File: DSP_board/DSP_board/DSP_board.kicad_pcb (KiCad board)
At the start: 2 copper layers, 67 parts, among them IC1 74LCX125MTCX, IC2 74LCX125MTCX, IC3 74LCX125MTCX, IC4 74LCX125MTCX, U1 AM264LAUNCH

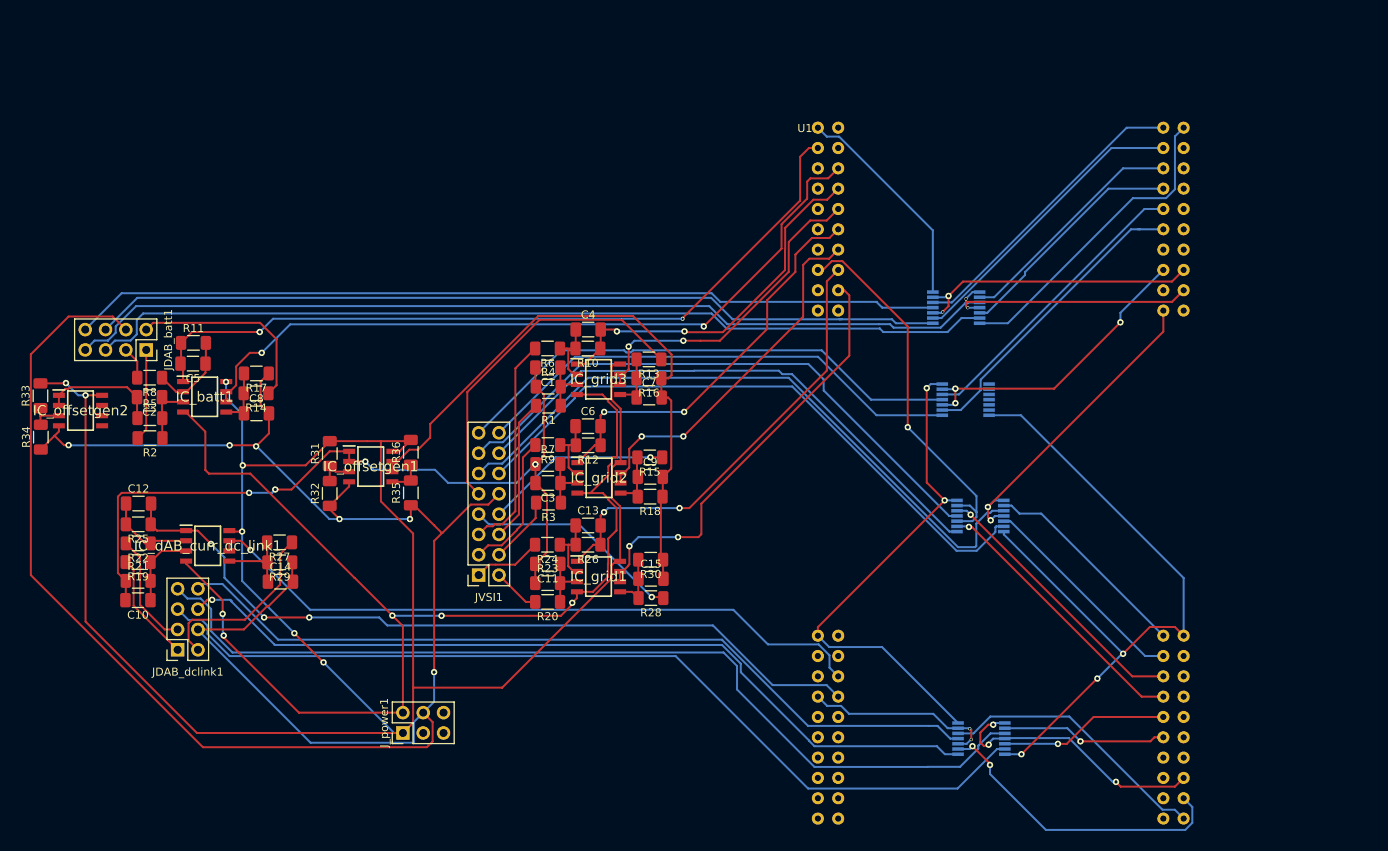
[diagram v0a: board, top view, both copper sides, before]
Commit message: including FPGA
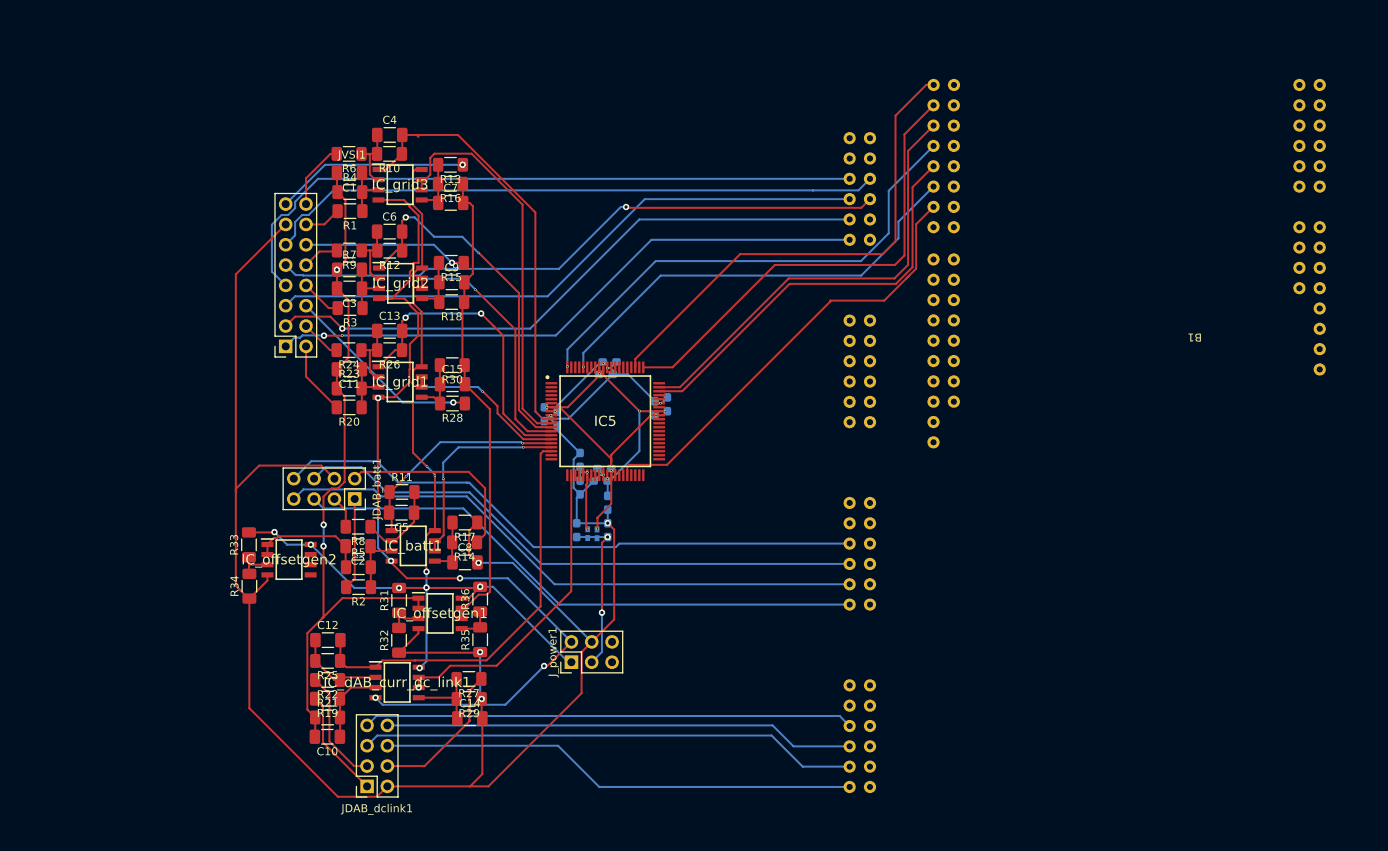
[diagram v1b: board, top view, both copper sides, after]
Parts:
- removed IC1, IC2, IC3, IC4: 74LCX125MTCX, 74125:SOP65P640X120-14N
- removed U1: AM264LAUNCH, am263x_devboard:AM2634_LAUNCH
- added B1: Arty-S7, Connector_PinHeader_2.54mm:Arty-S7, F.Cu at (211.8, 79.4)
- added C16: 10u, Capacitor_SMD:C_0603_1608Metric_Pad1.08x0.95mm_HandSolder, B.Cu at (133.3, 103.0)
- added C17: 10u, Capacitor_SMD:C_0603_1608Metric_Pad1.08x0.95mm_HandSolder, B.Cu at (133.3, 99.6)
- added C18: 2.2u, Capacitor_SMD:C_0603_1608Metric_Pad1.08x0.95mm_HandSolder, B.Cu at (129.4, 103.0)
- added Cvdd_1: 0.1u, Capacitor_SMD:C_0603_1608Metric_Pad1.08x0.95mm_HandSolder, B.Cu at (133.5, 81.9)
- added Cvdd_2: 0.1u, Capacitor_SMD:C_0603_1608Metric_Pad1.08x0.95mm_HandSolder, B.Cu at (132.4, 96.8)
- added Cvdd_3: 0.1u, Capacitor_SMD:C_0603_1608Metric_Pad1.08x0.95mm_HandSolder, B.Cu at (140.7, 87.2)
- added Cvdd_4: 0.1u, Capacitor_SMD:C_0603_1608Metric_Pad1.08x0.95mm_HandSolder, B.Cu at (127.0, 89.0)
- added Cvdda_1: 0.1u, Capacitor_SMD:C_0603_1608Metric_Pad1.08x0.95mm_HandSolder, B.Cu at (129.8, 94.2)
- added Cvdda_2: 0.1u, Capacitor_SMD:C_0603_1608Metric_Pad1.08x0.95mm_HandSolder, B.Cu at (129.8, 97.6)
- added Cvddio_1: 0.1u, Capacitor_SMD:C_0603_1608Metric_Pad1.08x0.95mm_HandSolder, B.Cu at (139.2, 87.7)
- added Cvddio_2: 0.1u, Capacitor_SMD:C_0603_1608Metric_Pad1.08x0.95mm_HandSolder, B.Cu at (132.8, 95.3)
- added Cvddio_3: 0.1u, Capacitor_SMD:C_0603_1608Metric_Pad1.08x0.95mm_HandSolder, B.Cu at (133.1, 83.5)
- added Cvddio_4: 0.1u, Capacitor_SMD:C_0603_1608Metric_Pad1.08x0.95mm_HandSolder, B.Cu at (125.4, 88.5)
- added FB1: BKP1005HS221-T, BKP100:BEADC1005X55N, B.Cu at (131.9, 103.4)
- added FB2: MPZ1005S600CT000, BKP100:BEADC1005X55N, B.Cu at (130.8, 103.4)
- added IC5: F280025CPNQR, f280025c:f280025c, F.Cu at (133.0, 89.4)
- moved JVSI1 37.4 mm to (93.0, 80.0)
- moved C15 34.7 mm to (113.9, 84.7)
- moved C4 34.7 mm to (106.0, 53.6)
- moved C7 34.7 mm to (113.7, 62.1)
- moved IC_grid2 34.7 mm to (107.4, 72.1)
- moved R13 34.7 mm to (113.6, 57.3)
- moved R16 34.7 mm to (113.6, 59.7)
- moved R24 34.7 mm to (100.9, 80.5)
- moved R28 34.7 mm to (113.9, 87.1)
- moved R30 34.7 mm to (113.8, 82.3)
- moved C11 34.7 mm to (101.0, 82.9)
- moved C13 34.7 mm to (106.0, 78.1)
- moved C3 34.7 mm to (101.0, 72.8)
- moved IC_grid1 34.7 mm to (107.3, 84.5)
- moved R1 34.7 mm to (101.1, 63.1)
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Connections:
- JDAB_batt1 pad 5: DAB2_PWM11 -> DAB2_PWM22
- JDAB_batt1 pad 6: DAB2_PWM21 -> DAB2_PWM12
- JDAB_batt1 pad 7: DAB2_PWM12 -> DAB2_PWM21
- JDAB_batt1 pad 8: DAB2_PWM22 -> DAB2_PWM11
- JDAB_dclink1 pad 2: V_dc_link -> ctrl_gnd
- JDAB_dclink1 pad 4: ctrl_gnd -> V_dc_link
- JDAB_dclink1 pad 5: DAB1PWM11 -> DAB1PWM21
- JDAB_dclink1 pad 6: DAB1PWM21 -> DAB1PWM22
- JDAB_dclink1 pad 7: DAB1PWM12 -> DAB1PWM11
- JDAB_dclink1 pad 8: DAB1PWM22 -> DAB1PWM12
- JVSI1 pad 1: Igrid1_ref -> VSI11
- JVSI1 pad 10: ctrl_gnd -> Igrid2_ref
- JVSI1 pad 11: VSI11 -> VSI32
- JVSI1 pad 12: VSI12 -> Vgrid2
- JVSI1 pad 13: VSI21 -> ctrl_gnd
- JVSI1 pad 14: VSI22 -> Igrid3
- JVSI1 pad 15: VSI31 -> Vgrid3
- JVSI1 pad 16: VSI32 -> Igrid3_ref
- JVSI1 pad 3: Igrid2_ref -> VSI12
- JVSI1 pad 4: Igrid2 -> Igrid1_ref
- JVSI1 pad 5: Igrid3_ref -> VSI21
- JVSI1 pad 6: Igrid3 -> Vgrid1
- JVSI1 pad 7: Vgrid1 -> VSI22
- JVSI1 pad 8: Vgrid2 -> Igrid2
- JVSI1 pad 9: Vgrid3 -> VSI31
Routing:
- net ctrl_15: track 261.9 -> 118.3 mm, vias 7 -> 9
- net /controller_sheet/gnd_buff1: track 90.8 -> 0.00 mm, vias 3 -> 0
- net batt_curr_sense: track 97.9 -> 27.8 mm
- net batt_V_sense: track 94.0 -> 26.1 mm
- net /controller_sheet/3v3_buf_1: track 64.2 -> 0.00 mm, vias 2 -> 0
- net /controller_sheet/pwmVSI1: track 0.00 -> 61.7 mm
- net /controller_sheet/pwm_daba1: track 0.00 -> 61.6 mm, vias 0 -> 1
- net DAB1PWM12: track 117.9 -> 58.9 mm
- net /controller_sheet/pwmVSI2: track 0.00 -> 58.7 mm
- net /controller_sheet/pwm_dabb2: track 0.00 -> 56.6 mm
- net /controller_sheet/pwmVSI3: track 0.00 -> 56.2 mm
- net /controller_sheet/pwm_dabb1: track 0.00 -> 55.4 mm, vias 0 -> 1
- net DAB1PWM11: track 115.3 -> 61.3 mm
- net /controller_sheet/pwm_daba2: track 0.00 -> 51.8 mm
- net /controller_sheet/vs1en2: track 47.9 -> 0.00 mm, vias 1 -> 0
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
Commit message: Connecting FPGA ADC pins
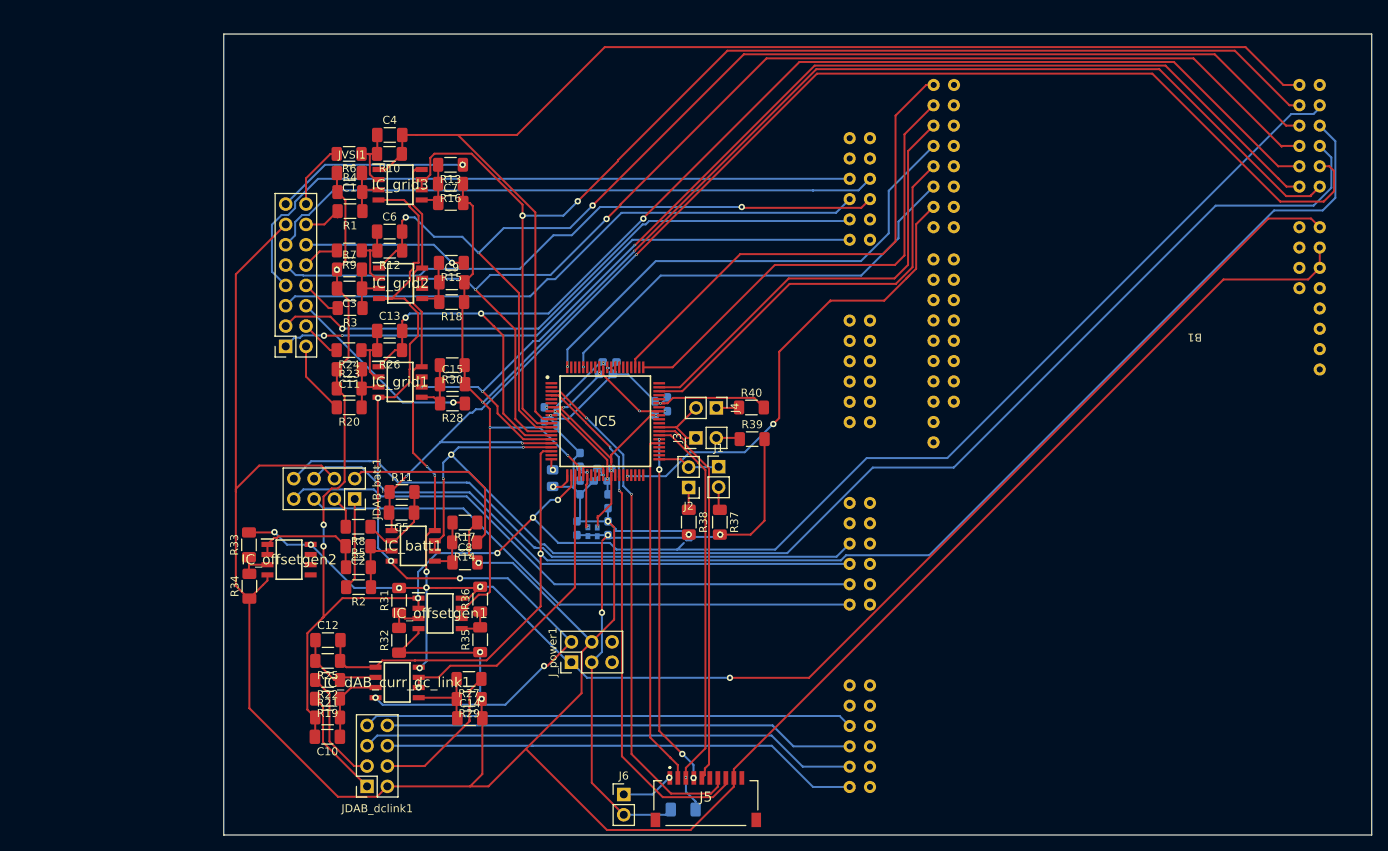
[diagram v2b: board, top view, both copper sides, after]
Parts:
- added C19: C, Capacitor_SMD:C_0805_2012Metric_Pad1.18x1.45mm_HandSolder, B.Cu at (126.4, 96.5)
- added J1: Conn_01x02, Connector_PinHeader_2.54mm:PinHeader_1x02_P2.54mm_Vertical, F.Cu at (147.1, 95.0)
- added J2: Conn_01x02, Connector_PinHeader_2.54mm:PinHeader_1x02_P2.54mm_Vertical, F.Cu at (143.4, 97.6)
- added J3: Conn_01x02, Connector_PinHeader_2.54mm:PinHeader_1x02_P2.54mm_Vertical, F.Cu at (144.3, 91.4)
- added J4: Conn_01x02, Connector_PinHeader_2.54mm:PinHeader_1x02_P2.54mm_Vertical, F.Cu at (146.9, 87.7)
- added J5: 1-84981-0, jtag_connector:1849810, F.Cu at (145.5, 136.3)
- added J6: Conn_01x02, Connector_PinHeader_2.54mm:PinHeader_1x02_P2.54mm_Vertical, F.Cu at (135.3, 136.0)
- added R37: R, Resistor_SMD:R_1206_3216Metric_Pad1.30x1.75mm_HandSolder, F.Cu at (147.3, 102.0)
- added R38: R, Resistor_SMD:R_1206_3216Metric_Pad1.30x1.75mm_HandSolder, F.Cu at (143.4, 102.0)
- added R39: R, Resistor_SMD:R_1206_3216Metric_Pad1.30x1.75mm_HandSolder, F.Cu at (151.3, 91.6)
- added R40: R, Resistor_SMD:R_1206_3216Metric_Pad1.30x1.75mm_HandSolder, F.Cu at (151.2, 87.6)
- added R41: R, Resistor_SMD:R_1206_3216Metric_Pad1.30x1.75mm_HandSolder, B.Cu at (142.7, 137.9)
- moved FB1 0.24 mm to (132.0, 103.2)
- moved FB2 0.24 mm to (130.8, 103.2)
- moved C16 0.24 mm to (133.3, 102.7)
- moved C18 0.24 mm to (129.4, 102.7)
- moved C17 0.19 mm to (133.3, 99.4)
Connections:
- B1 pad 14: unconnected-(B1-Pad14) -> offset_v
- B1 pad 15: unconnected-(B1-Pad15) -> batt_curr_sense
- B1 pad 16: unconnected-(B1-Pad16) -> batt_V_sense
- B1 pad 17: unconnected-(B1-Pad17) -> I_leackage
- B1 pad 18: unconnected-(B1-Pad18) -> offset_i
- B1 pad 20: unconnected-(B1-Pad20) -> Vgrid1_sense
- B1 pad 21: unconnected-(B1-Pad21) -> Igrid1_sense
- B1 pad 22: unconnected-(B1-Pad22) -> Vgrid2_sense
- B1 pad 23: unconnected-(B1-Pad23) -> Igrid2_sense
- B1 pad 24: unconnected-(B1-Pad24) -> Vgrid3_sense
- B1 pad 25: unconnected-(B1-Pad25) -> Igrid3_sense
- B1 pad 6: unconnected-(B1-Pad6) -> ctrl_gnd
- B1 pad 7: unconnected-(B1-Pad7) -> ctrl_gnd
- B1 pad 8: unconnected-(B1-Pad8) -> ctrl_15
- C1 pad 2: /curr_offset -> offset_i
- C10 pad 2: /curr_offset -> offset_i
- C11 pad 2: /curr_offset -> offset_i
- C15 pad 2: /voltage_offset -> offset_v
- C3 pad 2: /curr_offset -> offset_i
- C7 pad 2: /voltage_offset -> offset_v
- C9 pad 2: /voltage_offset -> offset_v
- IC5 pad 20: unconnected-(IC5-Pad20) -> Net-(IC5-Pad20)
- IC5 pad 21: unconnected-(IC5-Pad21) -> ctrl_gnd
- IC5 pad 22: Vdc_link -> offset_i
- IC5 pad 23: unconnected-(IC5-Pad23) -> Vdc_link
- IC5 pad 24: unconnected-(IC5-Pad24) -> offset_v
- IC5 pad 3: unconnected-(IC5-Pad3) -> SCITX
- IC5 pad 4: unconnected-(IC5-Pad4) -> SCiRX
- IC5 pad 41: unconnected-(IC5-Pad41) -> Net-(IC5-Pad41)
- IC5 pad 45: unconnected-(IC5-Pad45) -> TCK
- IC5 pad 46: unconnected-(IC5-Pad46) -> TDO
- IC5 pad 47: unconnected-(IC5-Pad47) -> TMS
- IC5 pad 48: unconnected-(IC5-Pad48) -> TDI
- IC5 pad 49: unconnected-(IC5-Pad49) -> Net-(IC5-Pad49)
- IC_offsetgen1 pad 1: /curr_offset -> offset_i
- IC_offsetgen1 pad 2: /curr_offset -> offset_i
- IC_offsetgen1 pad 6: /voltage_offset -> offset_v
- IC_offsetgen1 pad 7: /voltage_offset -> offset_v
- R16 pad 1: /voltage_offset -> offset_v
- R18 pad 1: /voltage_offset -> offset_v
- R21 pad 1: /curr_offset -> offset_i
- R23 pad 1: /curr_offset -> offset_i
- R30 pad 1: /voltage_offset -> offset_v
- R4 pad 1: /curr_offset -> offset_i
- R7 pad 1: /curr_offset -> offset_i
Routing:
- net offset_i: track 0.00 -> 245.4 mm, vias 0 -> 7
- net offset_v: track 0.00 -> 203.3 mm, vias 0 -> 4
- net ctrl_gnd: track 267.1 -> 434.1 mm, vias 8 -> 10
- net batt_curr_sense: track 27.8 -> 170.4 mm, vias 2 -> 3
- net batt_V_sense: track 26.1 -> 166.0 mm, vias 2 -> 3
- net I_leackage: track 51.7 -> 180.0 mm, vias 0 -> 1
- net Vgrid1_sense: track 22.1 -> 147.3 mm, vias 2 -> 3
- net Igrid1_sense: track 38.6 -> 159.4 mm, vias 2 -> 3
- net Vgrid2_sense: track 32.3 -> 151.9 mm, vias 2 -> 3
- net ctrl_15: track 118.3 -> 236.8 mm, vias 9 -> 10
- net Igrid2_sense: track 45.9 -> 162.4 mm, vias 2 -> 3
- net Igrid3_sense: track 54.1 -> 165.5 mm
- net Vgrid3_sense: track 49.0 -> 157.5 mm, vias 0 -> 2
- net /curr_offset: track 91.2 -> 0.00 mm, vias 3 -> 0
- net SCiRX: track 0.00 -> 66.1 mm, vias 0 -> 2
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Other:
- board outline added: 143.5 x 100.1 mm

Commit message: adding diodes
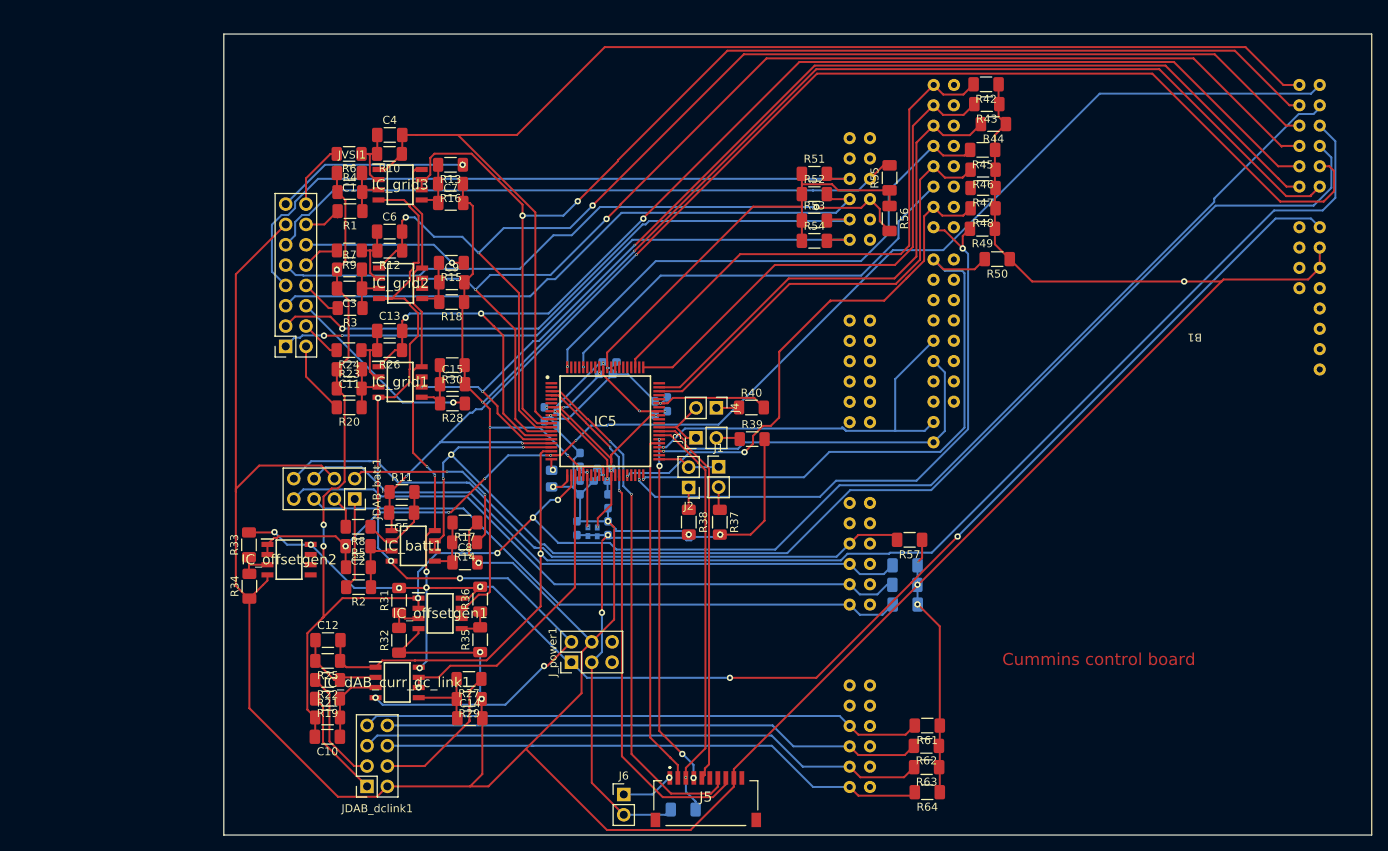
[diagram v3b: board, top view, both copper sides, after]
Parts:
- added R42: R, Capacitor_SMD:C_1206_3216Metric_Pad1.33x1.80mm_HandSolder, F.Cu at (180.6, 47.2)
- added R43: R, Capacitor_SMD:C_1206_3216Metric_Pad1.33x1.80mm_HandSolder, F.Cu at (180.7, 49.7)
- added R44: R, Capacitor_SMD:C_1206_3216Metric_Pad1.33x1.80mm_HandSolder, F.Cu at (181.5, 52.2)
- added R45: R, Capacitor_SMD:C_1206_3216Metric_Pad1.33x1.80mm_HandSolder, F.Cu at (180.1, 55.4)
- added R46: R, Capacitor_SMD:C_1206_3216Metric_Pad1.33x1.80mm_HandSolder, F.Cu at (180.2, 57.9)
- added R47: R, Capacitor_SMD:C_1206_3216Metric_Pad1.33x1.80mm_HandSolder, F.Cu at (180.2, 60.2)
- added R48: R, Capacitor_SMD:C_1206_3216Metric_Pad1.33x1.80mm_HandSolder, F.Cu at (180.2, 62.7)
- added R49: R, Capacitor_SMD:C_1206_3216Metric_Pad1.33x1.80mm_HandSolder, F.Cu at (180.1, 65.3)
- added R50: R, Capacitor_SMD:C_1206_3216Metric_Pad1.33x1.80mm_HandSolder, F.Cu at (182.0, 69.1)
- added R51: R, Capacitor_SMD:C_1206_3216Metric_Pad1.33x1.80mm_HandSolder, F.Cu at (159.1, 58.4)
- added R52: R, Capacitor_SMD:C_1206_3216Metric_Pad1.33x1.80mm_HandSolder, F.Cu at (159.1, 61.0)
- added R53: R, Capacitor_SMD:C_1206_3216Metric_Pad1.33x1.80mm_HandSolder, F.Cu at (159.1, 64.3)
- added R54: R, Capacitor_SMD:C_1206_3216Metric_Pad1.33x1.80mm_HandSolder, F.Cu at (159.1, 66.8)
- added R55: R, Capacitor_SMD:C_1206_3216Metric_Pad1.33x1.80mm_HandSolder, F.Cu at (168.5, 58.9)
- added R56: R, Capacitor_SMD:C_1206_3216Metric_Pad1.33x1.80mm_HandSolder, F.Cu at (168.5, 64.0)
- added R57: R, Capacitor_SMD:C_1206_3216Metric_Pad1.33x1.80mm_HandSolder, F.Cu at (171.0, 104.2)
- added R58: R, Capacitor_SMD:C_1206_3216Metric_Pad1.33x1.80mm_HandSolder, B.Cu at (170.4, 107.4)
- added R59: R, Capacitor_SMD:C_1206_3216Metric_Pad1.33x1.80mm_HandSolder, B.Cu at (170.4, 109.8)
- added R60: R, Capacitor_SMD:C_1206_3216Metric_Pad1.33x1.80mm_HandSolder, B.Cu at (170.5, 112.3)
- added R61: R, Capacitor_SMD:C_1206_3216Metric_Pad1.33x1.80mm_HandSolder, F.Cu at (173.2, 127.4)
- added R62: R, Capacitor_SMD:C_1206_3216Metric_Pad1.33x1.80mm_HandSolder, F.Cu at (173.1, 129.9)
- added R63: R, Capacitor_SMD:C_1206_3216Metric_Pad1.33x1.80mm_HandSolder, F.Cu at (173.1, 132.6)
- added R64: R, Capacitor_SMD:C_1206_3216Metric_Pad1.33x1.80mm_HandSolder, F.Cu at (173.2, 135.7)
- moved C19 0.14 mm to (126.3, 96.5)
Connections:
- B1 pad 19: unconnected-(B1-Pad19) -> batt_i_offset
- B1 pad 42: unconnected-(B1-Pad42) -> /controller_sheet/i2ca_sda
- B1 pad 43: unconnected-(B1-Pad43) -> /controller_sheet/i2ca_scl
- B1 pad 46: unconnected-(B1-Pad46) -> /controller_sheet/i2ca_sda
- B1 pad 47: unconnected-(B1-Pad47) -> /controller_sheet/i2ca_scl
- B1 pad 51: unconnected-(B1-Pad51) -> /controller_sheet/en_dab
- B1 pad 52: unconnected-(B1-Pad52) -> /controller_sheet/en_vsi
- C2 pad 2: /batt_curr_offset -> batt_i_offset
- IC5 pad 19: unconnected-(IC5-Pad19) -> batt_i_offset
- IC5 pad 39: unconnected-(IC5-Pad39) -> /controller_sheet/en_vsi
- IC5 pad 40: unconnected-(IC5-Pad40) -> /controller_sheet/en_dab
- IC5 pad 43: unconnected-(IC5-Pad43) -> /controller_sheet/i2ca_sda
- IC5 pad 44: unconnected-(IC5-Pad44) -> /controller_sheet/i2ca_scl
- IC_offsetgen2 pad 1: /batt_curr_offset -> batt_i_offset
- IC_offsetgen2 pad 2: /batt_curr_offset -> batt_i_offset
- R5 pad 1: /batt_curr_offset -> batt_i_offset
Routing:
- net batt_i_offset: track 0.00 -> 160.2 mm, vias 0 -> 5
- net ctrl_gnd: track 434.1 -> 572.6 mm, vias 10 -> 14
- net /controller_sheet/en_vsi: track 0.00 -> 76.1 mm, vias 0 -> 2
- net /controller_sheet/en_dab: track 0.00 -> 74.2 mm, vias 0 -> 1
- net /controller_sheet/i2ca_scl: track 0.00 -> 49.3 mm, vias 0 -> 1
- net /controller_sheet/i2ca_sda: track 0.00 -> 45.6 mm, vias 0 -> 1
- net /batt_curr_offset: track 14.6 -> 0.00 mm
- net DAB1PWM21: track 62.5 -> 71.6 mm
- net DAB1PWM11: track 61.3 -> 70.4 mm
- net DAB1PWM12: track 58.9 -> 67.8 mm
- net DAB1PWM22: track 60.3 -> 69.0 mm
- net /controller_sheet/pwmVSI3: track 56.2 -> 63.2 mm
- net /controller_sheet/pwmVSI1: track 61.7 -> 68.5 mm
- net DAB2_PWM11: track 76.1 -> 82.7 mm
- net DAB2_PWM22: track 72.4 -> 78.8 mm
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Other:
- board text added: "Cummins control board"

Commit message: save
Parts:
- added U1: SN74S1053NSR, diodes:SOIC127P780X200-20N, F.Cu at (114.2, 45.2)
